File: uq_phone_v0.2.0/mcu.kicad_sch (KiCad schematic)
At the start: 41 parts, among them J6 Conn_ARM_SWD_TagConnect_TC2030, J7 559092474, J9 559092474, Q1 MMBT3904LP-7, Q2 MMBT3904LP-7, U17 TXU0204DTRR, U18 TXU0304DTRR, U19 TXU0104DTRR, U20 TXU0104DTRR, U5 TCA9509MRVHR, U6 STM32H723VGHx

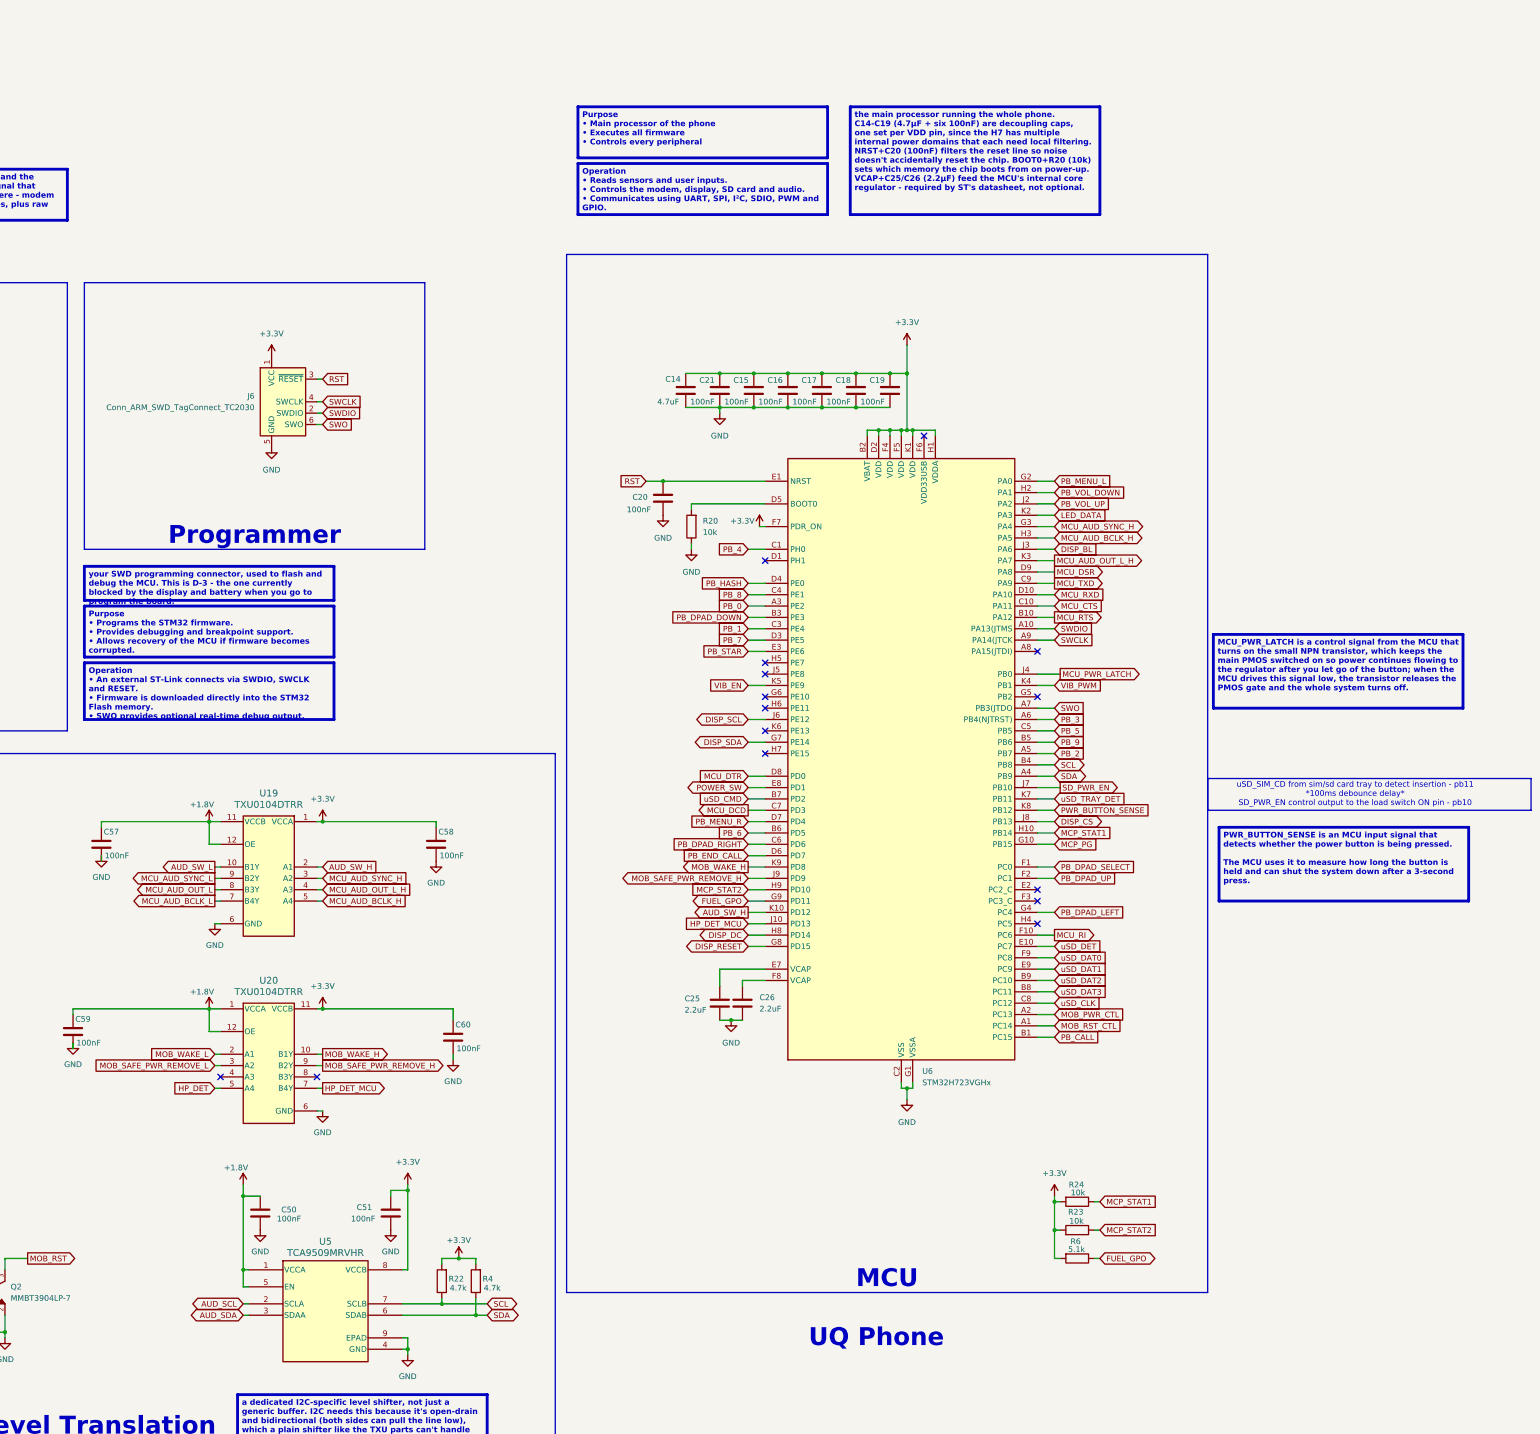
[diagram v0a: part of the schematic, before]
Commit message: Complete STM32H723ZGI6 144-pin schematic and FMC mapping
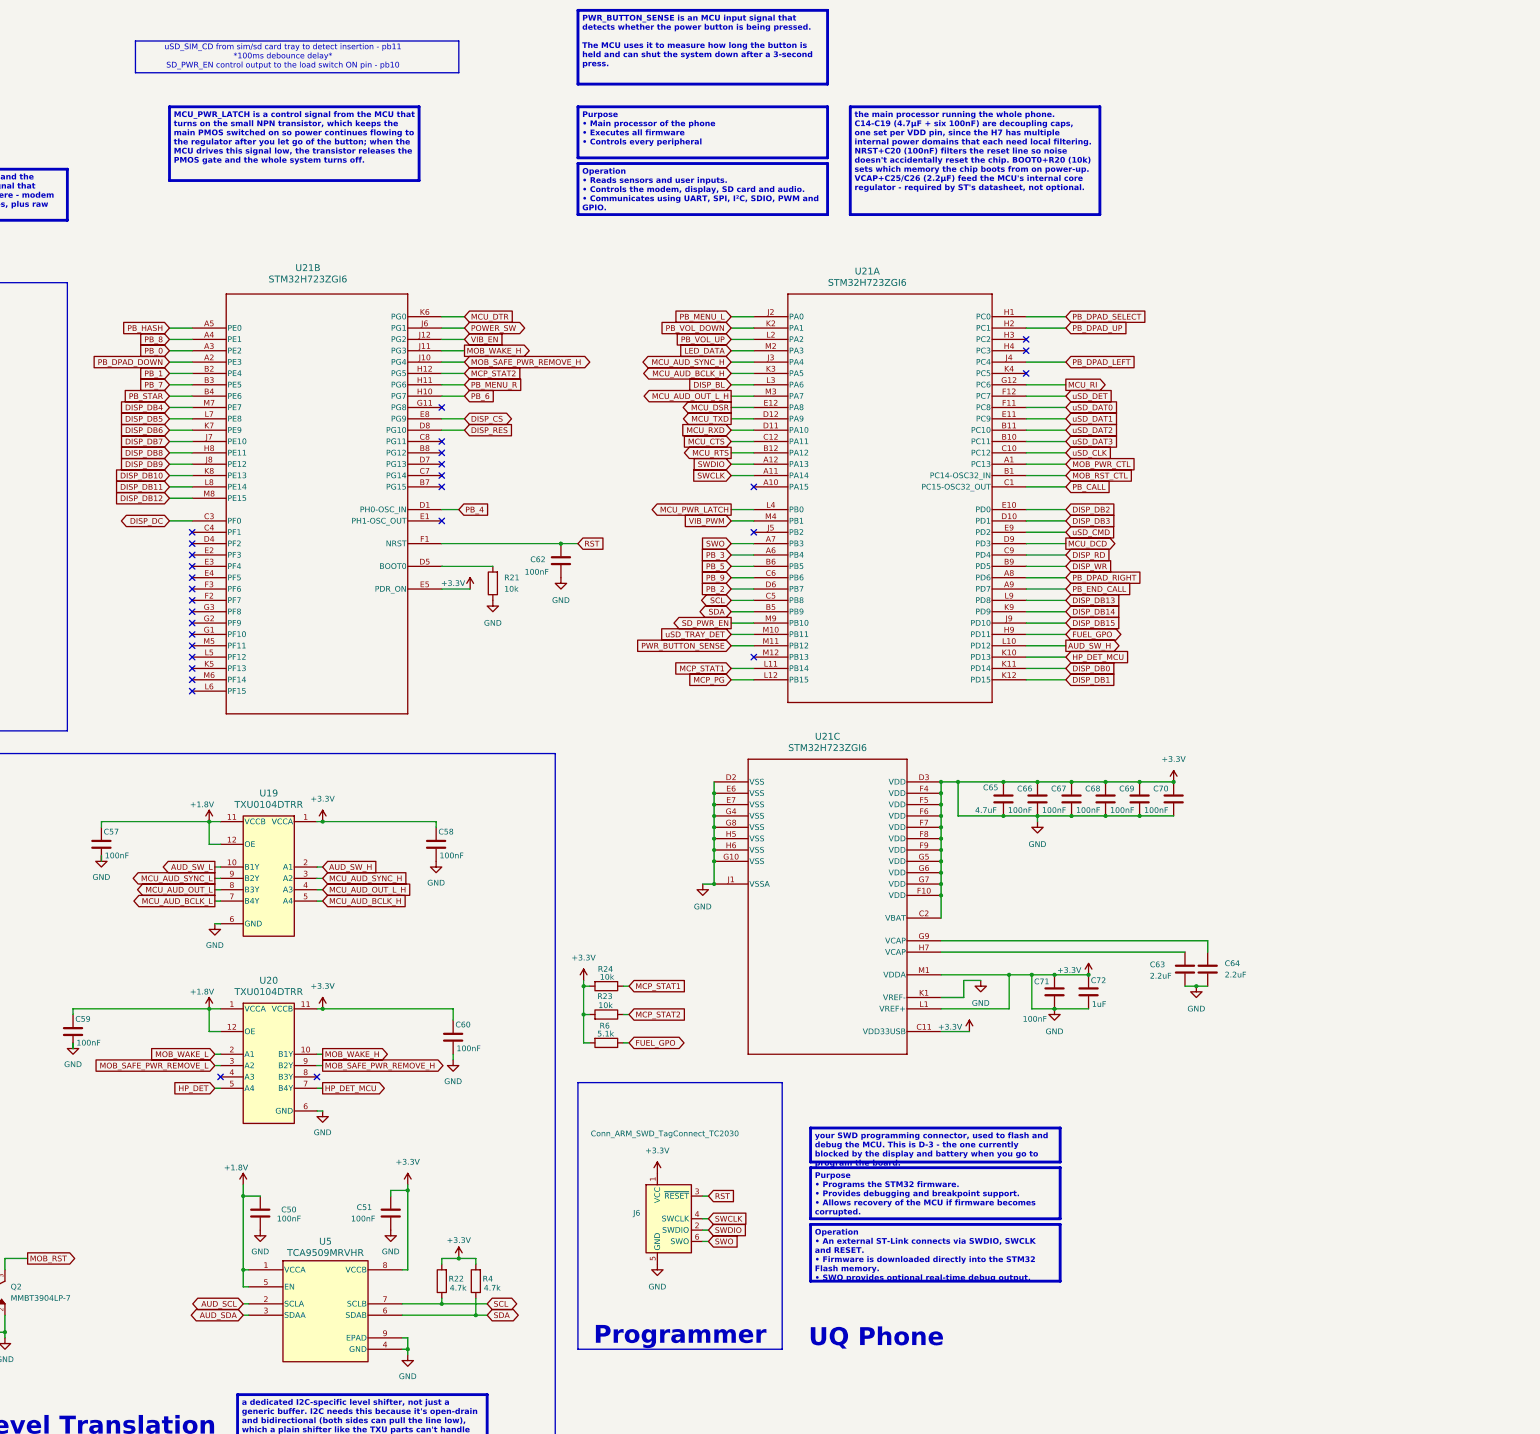
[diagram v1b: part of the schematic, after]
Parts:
- removed C14: 4.7uF, Capacitor_SMD:C_0201_0603Metric, symbol Capacitors:Capacitor_4.7uF
- removed C15, C16, C17, C18, C19, C20, C21: 100nF, Capacitor_SMD:C_0201_0603Metric, symbol Capacitors:capacitor_100nF
- removed C25, C26: 2.2uF, Capacitor_SMD:C_0402_1005Metric, symbol Capacitors:Capacitor_2.2uF
- removed R20: 10k, Resistor_SMD:R_0201_0603Metric, symbol Resistors:Resistor_10k
- removed U6: STM32H723VGHx, Package_BGA:TFBGA-100_8x8mm_Layout10x10_P0.8mm, symbol MCU_ST_STM32H7:STM32H723VGHx
- added C62, C66, C67, C68, C69, C70, C71: 100nF, Capacitor_SMD:C_0201_0603Metric, symbol Capacitors:capacitor_100nF
- added C63, C64: 2.2uF, Capacitor_SMD:C_0402_1005Metric, symbol Capacitors:Capacitor_2.2uF
- added C65: 4.7uF, Capacitor_SMD:C_0201_0603Metric, symbol Capacitors:Capacitor_4.7uF
- added C72: 1uF, Capacitor_SMD:C_0201_0603Metric, symbol Capacitors:Capacitor_1uF
- added R21: 10k, Resistor_SMD:R_0201_0603Metric, symbol Resistors:Resistor_10k
- added U21: STM32H723ZGI6, UFBGA-144_7X7_STM, symbol STM32H723ZGI6 UFBGA144:STM32H723ZGI6
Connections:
- net GND is gone; now on net +3.3V: C28.2, C50.2, C51.2, C54.2, C55.2, C56.2, C57.2, C58.2, C59.2, C60.2, J6.5 (GND), J7.1, J7.10, J7.11, J7.12, J7.2, J7.24, J7.3, J7.4, J7.5, J7.6, J7.7, J7.8, J7.9, J7.P1, J7.P2, J7.P3, J7.P4, J9.5, J9.6, J9.7, J9.8, J9.P1, J9.P2, J9.P3, J9.P4, Q1.2, Q2.2, R18.1, R19.1, U17.6 (GND), U18.6 (GND), U19.6 (GND), U20.6 (GND), U5.4 (GND), U5.9 (EPAD)
- net +3.3V: now also C62.1, C63.2, C64.2, C65.1, C65.2, C66.1, C66.2, C67.1, C67.2, C68.1, C68.2, C69.1, C69.2, C70.1, C70.2, C71.1, C71.2, C72.1, C72.2, R21.1, U21.C11 (VDD33USB), U21.C2 (VBAT), U21.D2 (VSS), U21.D3 (VDD), U21.E5 (PDR_ON), U21.E6 (VSS), U21.E7 (VSS), U21.F10 (VDD), U21.F4 (VDD), U21.F5 (VDD), U21.F6 (VDD), U21.F7 (VDD), U21.F8 (VDD), U21.F9 (VDD), U21.G10 (VSS), U21.G4 (VSS), U21.G5 (VDD), U21.G6 (VDD), U21.G7 (VDD), U21.G8 (VSS), U21.H5 (VSS), U21.H6 (VSS), U21.J1 (VSSA), U21.K1 (VREF-), U21.L1 (VREF+), U21.M1 (VDDA)
- net AUD_SW_H: now also U21.L10 (PD12)
- net DISP_BL: now also U21.L3 (PA6)
- net DISP_CS: now also U21.E8 (PG9)
- net DISP_DC: now also U21.C3 (PF0)
- net FUEL_GPO: now also U21.H9 (PD11)
- net HP_DET_MCU: now also U21.K10 (PD13)
- net LED_DATA: now also U21.M2 (PA3)
- net MCP_PG: now also U21.L12 (PB15)
- net MCP_STAT1: now also U21.L11 (PB14)
- net MCP_STAT2: now also U21.H12 (PG5)
- net MCU_AUD_BCLK_H: now also U21.K3 (PA5)
- net MCU_AUD_OUT_L_H: now also U21.M3 (PA7)
- net MCU_AUD_SYNC_H: now also U21.J3 (PA4)
- net MCU_CTS: now also U21.C12 (PA11)
- net MCU_DCD: now also U21.D9 (PD3)
- net MCU_DSR: now also U21.E12 (PA8)
- net MCU_DTR: now also U21.K6 (PG0)
- net MCU_PWR_LATCH: now also U21.L4 (PB0)
- net MCU_RI: now also U21.G12 (PC6)
- net MCU_RTS: now also U21.B12 (PA12)
- net MCU_RXD: now also U21.D11 (PA10)
- net MCU_TXD: now also U21.D12 (PA9)
- net MOB_PWR_CTL: now also U21.A1 (PC13)
- net MOB_RST_CTL: now also U21.B1 (PC14-OSC32_IN)
- net MOB_SAFE_PWR_REMOVE_H: now also U21.J10 (PG4)
- net MOB_WAKE_H: now also U21.J11 (PG3)
- net PB_0: now also U21.A3 (PE2)
- net PB_1: now also U21.B2 (PE4)
- net PB_2: now also U21.D6 (PB7)
- net PB_3: now also U21.A6 (PB4)
- net PB_4: now also U21.D1 (PH0-OSC_IN)
- net PB_5: now also U21.B6 (PB5)
- net PB_6: now also U21.H10 (PG7)
- net PB_7: now also U21.B3 (PE5)
- net PB_8: now also U21.A4 (PE1)
- net PB_9: now also U21.C6 (PB6)
- net PB_CALL: now also U21.C1 (PC15-OSC32_OUT)
- net PB_DPAD_DOWN: now also U21.A2 (PE3)
- net PB_DPAD_LEFT: now also U21.J4 (PC4)
- net PB_DPAD_RIGHT: now also U21.A8 (PD6)
- net PB_DPAD_SELECT: now also U21.H1 (PC0)
- net PB_DPAD_UP: now also U21.H2 (PC1)
- net PB_END_CALL: now also U21.A9 (PD7)
- net PB_HASH: now also U21.A5 (PE0)
- net PB_MENU_L: now also U21.J2 (PA0)
- net PB_MENU_R: now also U21.H11 (PG6)
- net PB_STAR: now also U21.B4 (PE6)
- net PB_VOL_DOWN: now also U21.K2 (PA1)
- net PB_VOL_UP: now also U21.L2 (PA2)
- net POWER_SW: now also U21.J6 (PG1)
- net PWR_BUTTON_SENSE: now also U21.M11 (PB12)
- net RST: now also C62.2, U21.F1 (NRST)
- net SCL: now also U21.C5 (PB8)
- net SDA: now also U21.B5 (PB9)
- net SD_PWR_EN: now also U21.M9 (PB10)
- net SWCLK: now also U21.A11 (PA14)
- net SWDIO: now also U21.A12 (PA13)
- net SWO: now also U21.A7 (PB3)
- net VIB_EN: now also U21.J12 (PG2)
- net VIB_PWM: now also U21.M4 (PB1)
- net uSD_CLK: now also U21.C10 (PC12)
- net uSD_CMD: now also U21.E9 (PD2)
- net uSD_DAT0: now also U21.F11 (PC8)
- net uSD_DAT1: now also U21.E11 (PC9)
- net uSD_DAT2: now also U21.B11 (PC10)
- net uSD_DAT3: now also U21.B10 (PC11)
- net uSD_DET: now also U21.F12 (PC7)
- net uSD_TRAY_DET: now also U21.M10 (PB11)
- new net: C64.1, U21.G9 (VCAP)
- new net: C63.1, U21.H7 (VCAP)
- new net: R21.2, U21.D5 (BOOT0)
- new net DISP_DB0: U21.K11 (PD14)
- new net DISP_DB1: U21.K12 (PD15)
- new net DISP_DB10: U21.K8 (PE13)
- new net DISP_DB11: U21.L8 (PE14)
- new net DISP_DB12: U21.M8 (PE15)
- new net DISP_DB13: U21.L9 (PD8)
- new net DISP_DB14: U21.K9 (PD9)
- new net DISP_DB15: U21.J9 (PD10)
- new net DISP_DB2: U21.E10 (PD0)
- new net DISP_DB3: U21.D10 (PD1)
- new net DISP_DB4: U21.M7 (PE7)
- new net DISP_DB5: U21.L7 (PE8)
- new net DISP_DB6: U21.K7 (PE9)
- new net DISP_DB7: U21.J7 (PE10)
- new net DISP_DB8: U21.H8 (PE11)
- new net DISP_DB9: U21.J8 (PE12)
- new net DISP_RD: U21.C9 (PD4)
- new net DISP_RES: U21.D8 (PG10)
- new net DISP_WR: U21.B9 (PD5)
- no-connect marks 15 -> 30
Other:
- moved on the sheet: J6, R23, R24, R6
